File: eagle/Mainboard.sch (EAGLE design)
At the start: 34 parts, among them IC1 L293D, IC2 TLC272P, IC3 LM1085IT-5.0

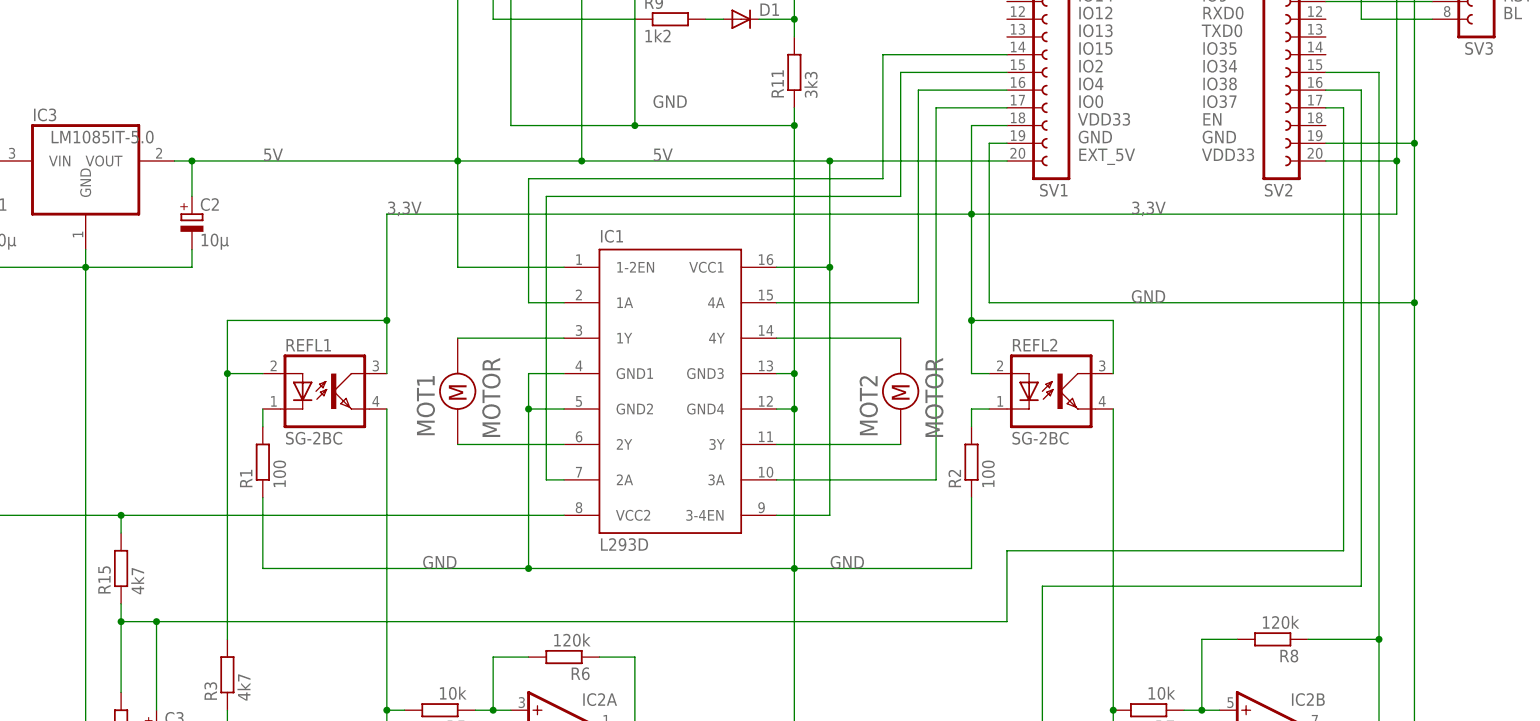
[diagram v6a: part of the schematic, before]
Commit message: 5V-Jumper hinzugefügt und Spanungsteiler für Akkumessung angepasst
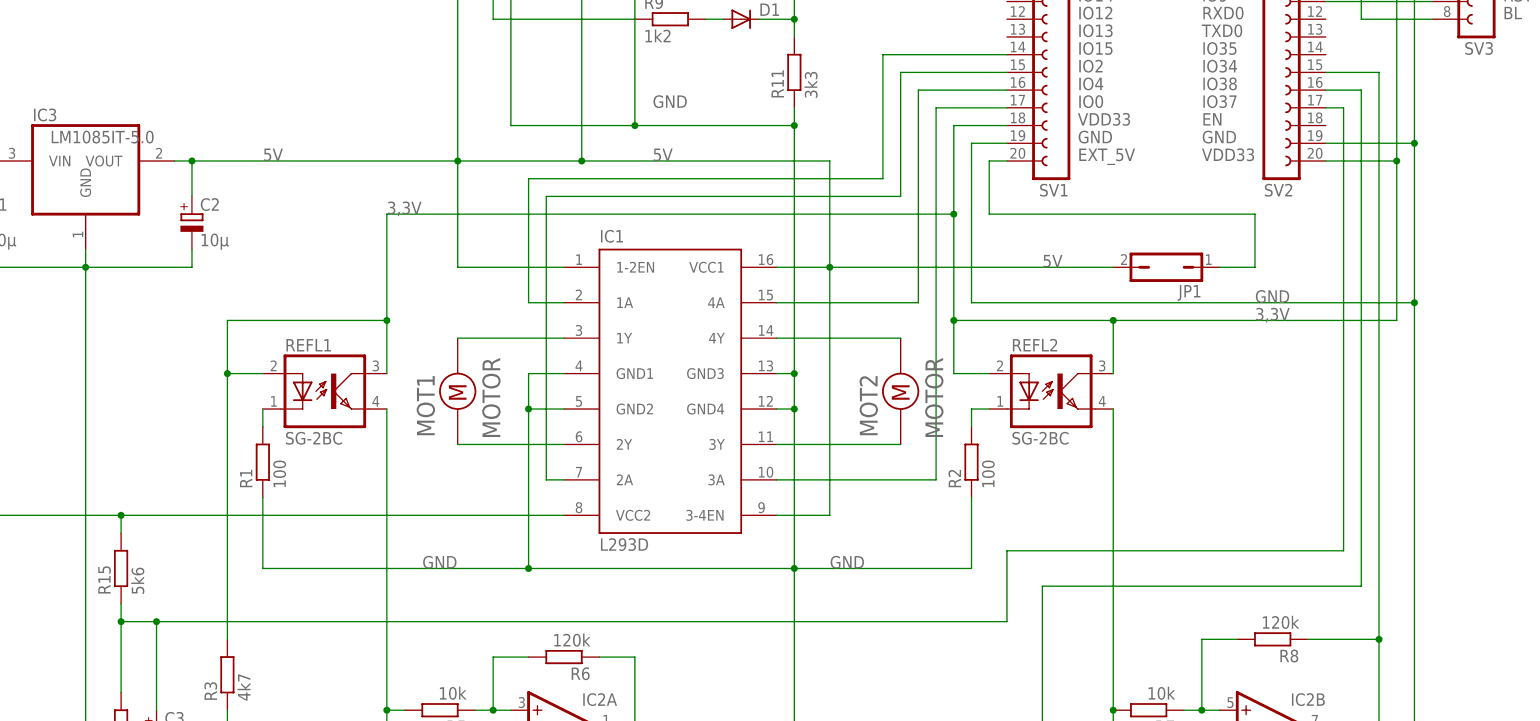
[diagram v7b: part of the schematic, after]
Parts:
- added JP1: (no value), jumper:JP1Q
- R15: value 4k7 -> 5k6
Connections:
- new net N$27: JP1.1, SV1.20
- net 5V: now also JP1.2; no longer SV1.20
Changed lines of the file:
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@@
 <part name="C3" library="rcl" library_urn="urn:adsk.eagle:library:334" deviceset="CPOL-EU" device="E3.5-10" package3d_urn="urn:adsk.eagle:package:23351/1" value="10µ"/>
 <part name="R14" library="rcl" library_urn="urn:adsk.eagle:library:334" deviceset="R-EU_" device="RDH/15" package3d_urn="urn:adsk.eagle:package:23595/1" value="3k3"/>
-<part name="R15" library="rcl" library_urn="urn:adsk.eagle:library:334" deviceset="R-EU_" device="RDH/15" package3d_urn="urn:adsk.eagle:package:23595/1" value="4k7"/>
+<part name="R15" library="rcl" library_urn="urn:adsk.eagle:library:334" deviceset="R-EU_" device="RDH/15" package3d_urn="urn:adsk.eagle:package:23595/1" value="5k6"/>
+<part name="JP1" library="jumper" library_urn="urn:adsk.eagle:library:252" deviceset="JP1Q" device="" package3d_urn="urn:adsk.eagle:package:15455/1"/>
 </parts>
 <sheets>
@@
 <instance part="R14" gate="G$1" x="25.4" y="25.4" rot="R90"/>
 <instance part="R15" gate="G$1" x="25.4" y="48.26" rot="R90"/>
+<instance part="JP1" gate="A" x="175.26" y="91.44" rot="R90"/>
 </instances>
 <busses>
@@
 <wire x1="121.92" y1="48.26" x2="147.32" y2="48.26" width="0.1524" layer="91"/>
 <wire x1="147.32" y1="48.26" x2="147.32" y2="58.42" width="0.1524" layer="91"/>
-<wire x1="149.86" y1="86.36" x2="210.82" y2="86.36" width="0.1524" layer="91"/>
+<wire x1="147.32" y1="86.36" x2="210.82" y2="86.36" width="0.1524" layer="91"/>
 <wire x1="210.82" y1="86.36" x2="210.82" y2="109.22" width="0.1524" layer="91"/>
 <pinref part="SV2" gate="G$1" pin="19"/>
@@
 <wire x1="210.82" y1="142.24" x2="213.36" y2="142.24" width="0.1524" layer="91"/>
 <pinref part="SV1" gate="G$1" pin="19"/>
-<wire x1="152.4" y1="109.22" x2="149.86" y2="109.22" width="0.1524" layer="91"/>
-<wire x1="149.86" y1="86.36" x2="149.86" y2="109.22" width="0.1524" layer="91"/>
-<label x="170.18" y="86.36" size="1.778" layer="95"/>
+<wire x1="152.4" y1="109.22" x2="147.32" y2="109.22" width="0.1524" layer="91"/>
+<wire x1="147.32" y1="86.36" x2="147.32" y2="109.22" width="0.1524" layer="91"/>
+<label x="187.96" y="86.36" size="1.778" layer="95"/>
 <label x="149.86" y="5.08" size="1.778" layer="95"/>
 <pinref part="R11" gate="G$1" pin="1"/>
@@
 <wire x1="35.56" y1="106.68" x2="73.66" y2="106.68" width="0.1524" layer="91"/>
 <wire x1="73.66" y1="106.68" x2="91.44" y2="106.68" width="0.1524" layer="91"/>
-<pinref part="SV1" gate="G$1" pin="20"/>
 <wire x1="91.44" y1="106.68" x2="127" y2="106.68" width="0.1524" layer="91"/>
-<wire x1="127" y1="106.68" x2="152.4" y2="106.68" width="0.1524" layer="91"/>
-<junction x="127" y="106.68"/>
 <pinref part="US1" gate="A" pin="1"/>
 <wire x1="73.66" y1="149.86" x2="73.66" y2="106.68" width="0.1524" layer="91"/>
@@
 <wire x1="35.56" y1="101.6" x2="35.56" y2="106.68" width="0.1524" layer="91"/>
 <junction x="35.56" y="106.68"/>
+<pinref part="JP1" gate="A" pin="2"/>
+<wire x1="127" y1="91.44" x2="167.64" y2="91.44" width="0.1524" layer="91"/>
+<label x="157.48" y="91.44" size="1.778" layer="95"/>
 </segment>
 </net>
@@
 <segment>
 <pinref part="SV1" gate="G$1" pin="18"/>
-<wire x1="152.4" y1="111.76" x2="147.32" y2="111.76" width="0.1524" layer="91"/>
-<wire x1="147.32" y1="111.76" x2="147.32" y2="99.06" width="0.1524" layer="91"/>
-<wire x1="147.32" y1="99.06" x2="208.28" y2="99.06" width="0.1524" layer="91"/>
-<wire x1="208.28" y1="99.06" x2="208.28" y2="106.68" width="0.1524" layer="91"/>
+<wire x1="152.4" y1="111.76" x2="144.78" y2="111.76" width="0.1524" layer="91"/>
+<wire x1="144.78" y1="111.76" x2="144.78" y2="99.06" width="0.1524" layer="91"/>
 <pinref part="SV2" gate="G$1" pin="20"/>
 <wire x1="208.28" y1="106.68" x2="198.12" y2="106.68" width="0.1524" layer="91"/>
@@
 <wire x1="63.5" y1="99.06" x2="63.5" y2="83.82" width="0.1524" layer="91"/>
 <wire x1="63.5" y1="83.82" x2="63.5" y2="76.2" width="0.1524" layer="91"/>
-<wire x1="147.32" y1="99.06" x2="63.5" y2="99.06" width="0.1524" layer="91"/>
-<junction x="147.32" y="99.06"/>
+<wire x1="144.78" y1="99.06" x2="63.5" y2="99.06" width="0.1524" layer="91"/>
+<junction x="144.78" y="99.06"/>
 <pinref part="REFL2" gate="G$1" pin="A"/>
-<wire x1="149.86" y1="76.2" x2="147.32" y2="76.2" width="0.1524" layer="91"/>
-<wire x1="147.32" y1="76.2" x2="147.32" y2="83.82" width="0.1524" layer="91"/>
-<wire x1="147.32" y1="83.82" x2="167.64" y2="83.82" width="0.1524" layer="91"/>
+<wire x1="149.86" y1="76.2" x2="144.78" y2="76.2" width="0.1524" layer="91"/>
+<wire x1="144.78" y1="76.2" x2="144.78" y2="83.82" width="0.1524" layer="91"/>
+<wire x1="144.78" y1="83.82" x2="167.64" y2="83.82" width="0.1524" layer="91"/>
 <wire x1="167.64" y1="83.82" x2="167.64" y2="76.2" width="0.1524" layer="91"/>
 <pinref part="REFL2" gate="G$1" pin="COL"/>
-<wire x1="147.32" y1="99.06" x2="147.32" y2="83.82" width="0.1524" layer="91"/>
-<junction x="147.32" y="83.82"/>
-<label x="170.18" y="99.06" size="1.778" layer="95"/>
+<wire x1="144.78" y1="99.06" x2="144.78" y2="83.82" width="0.1524" layer="91"/>
+<junction x="144.78" y="83.82"/>
+<label x="187.96" y="83.82" size="1.778" layer="95"/>
 <wire x1="208.28" y1="106.68" x2="208.28" y2="144.78" width="0.1524" layer="91"/>
 <junction x="208.28" y="106.68"/>
@@
 <wire x1="40.64" y1="83.82" x2="63.5" y2="83.82" width="0.1524" layer="91"/>
 <junction x="63.5" y="83.82"/>
+<wire x1="167.64" y1="83.82" x2="208.28" y2="83.82" width="0.1524" layer="91"/>
+<junction x="167.64" y="83.82"/>
+<wire x1="208.28" y1="83.82" x2="208.28" y2="106.68" width="0.1524" layer="91"/>
 </segment>
 </net>
@@
 </segment>
 </net>
+<net name="N$27" class="0">
+<segment>
+<pinref part="SV1" gate="G$1" pin="20"/>
+<wire x1="152.4" y1="106.68" x2="149.86" y2="106.68" width="0.1524" layer="91"/>
+<wire x1="149.86" y1="106.68" x2="149.86" y2="99.06" width="0.1524" layer="91"/>
+<wire x1="149.86" y1="99.06" x2="187.96" y2="99.06" width="0.1524" layer="91"/>
+<wire x1="187.96" y1="99.06" x2="187.96" y2="91.44" width="0.1524" layer="91"/>
+<pinref part="JP1" gate="A" pin="1"/>
+<wire x1="187.96" y1="91.44" x2="182.88" y2="91.44" width="0.1524" layer="91"/>
+</segment>
+</net>

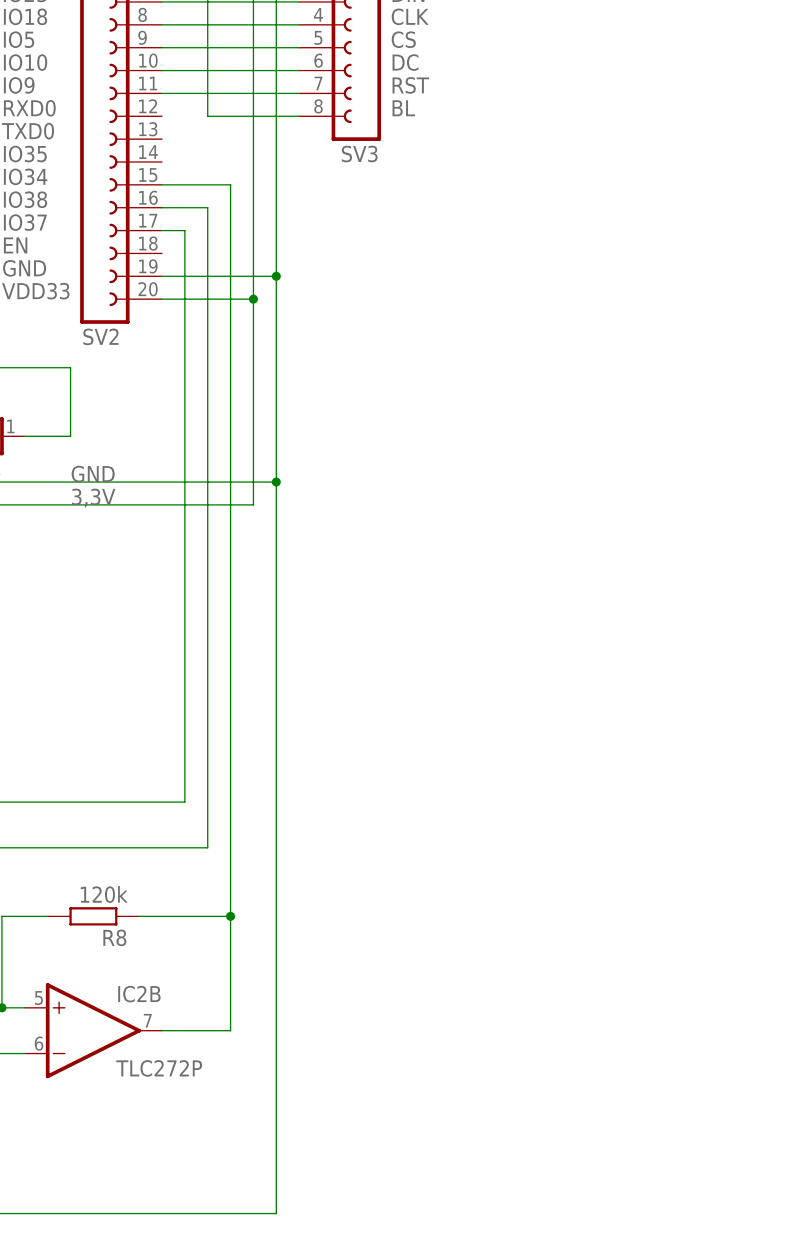
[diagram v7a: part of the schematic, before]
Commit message: Wassersensor hinzugefügt
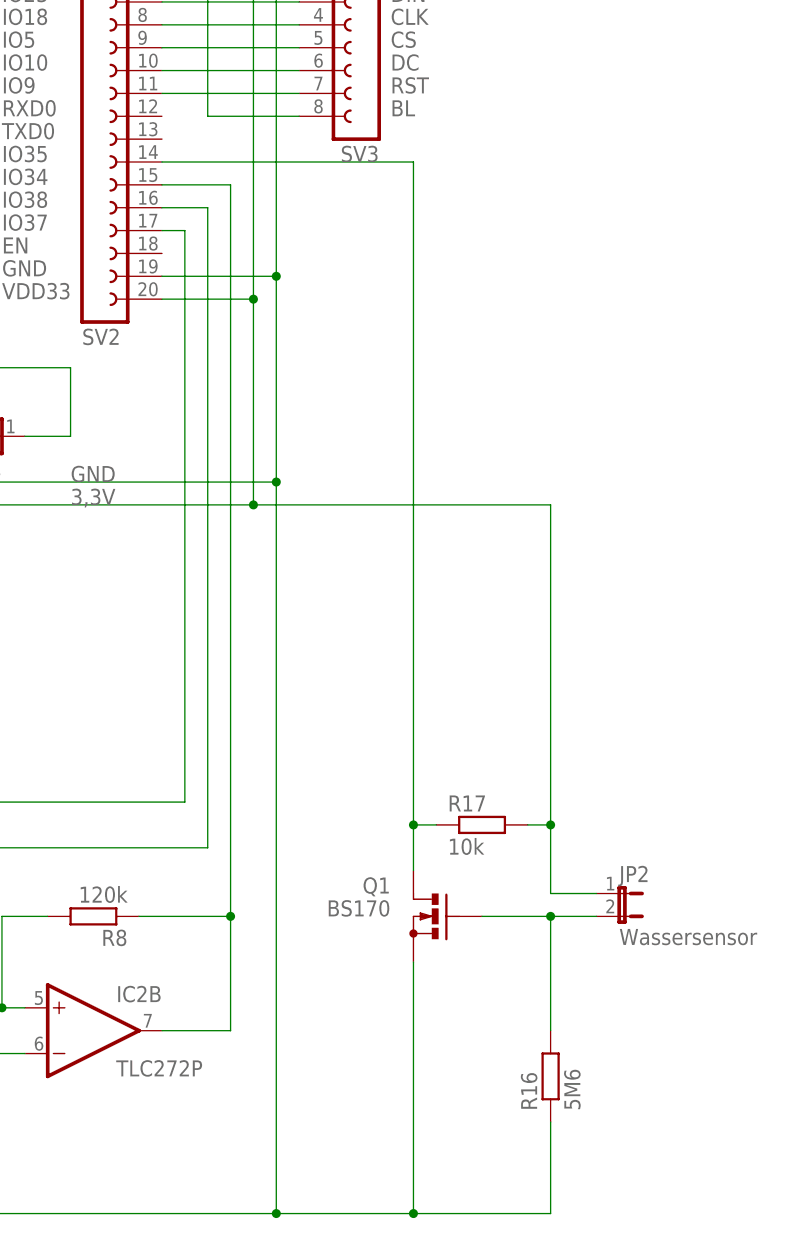
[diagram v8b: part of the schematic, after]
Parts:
- added JP2: Wassersensor, jumper:JP1E
- added Q1: BS170, transistor-small-signal:BS170
- added R16: 5M6, rcl:R-EU_RDH/15
- added R17: 10k, rcl:R-EU_RDH/15
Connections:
- new net N$34: Q1.D, R17.1, SV2.14
- new net N$35: JP2.2, Q1.G, R16.2
- net 3,3V: now also JP2.1, R17.2
- net GND: now also Q1.S, R16.1
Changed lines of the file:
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@@
 <part name="R15" library="rcl" library_urn="urn:adsk.eagle:library:334" deviceset="R-EU_" device="RDH/15" package3d_urn="urn:adsk.eagle:package:23595/1" value="5k6"/>
 <part name="JP1" library="jumper" library_urn="urn:adsk.eagle:library:252" deviceset="JP1Q" device="" package3d_urn="urn:adsk.eagle:package:15455/1"/>
+<part name="Q1" library="transistor-small-signal" library_urn="urn:adsk.eagle:library:401" deviceset="BS170" device="" package3d_urn="urn:adsk.eagle:package:29751/1"/>
+<part name="R16" library="rcl" library_urn="urn:adsk.eagle:library:334" deviceset="R-EU_" device="RDH/15" package3d_urn="urn:adsk.eagle:package:23595/1" value="5M6"/>
+<part name="JP2" library="jumper" library_urn="urn:adsk.eagle:library:252" deviceset="JP1E" device="" package3d_urn="urn:adsk.eagle:package:15455/1" value="Wassersensor"/>
+<part name="R17" library="rcl" library_urn="urn:adsk.eagle:library:334" deviceset="R-EU_" device="RDH/15" package3d_urn="urn:adsk.eagle:package:23595/1" value="10k"/>
 </parts>
 <sheets>
@@
 <instance part="R15" gate="G$1" x="25.4" y="48.26" rot="R90"/>
 <instance part="JP1" gate="A" x="175.26" y="91.44" rot="R90"/>
+<instance part="Q1" gate="1" x="228.6" y="38.1" rot="MR0"/>
+<instance part="R16" gate="G$1" x="241.3" y="20.32" rot="R90"/>
+<instance part="JP2" gate="A" x="248.92" y="40.64" rot="R270"/>
+<instance part="R17" gate="G$1" x="233.68" y="48.26"/>
 </instances>
 <busses>
@@
 <wire x1="25.4" y1="20.32" x2="25.4" y2="5.08" width="0.1524" layer="91"/>
 <junction x="25.4" y="5.08"/>
+<pinref part="Q1" gate="1" pin="S"/>
+<wire x1="226.06" y1="33.02" x2="226.06" y2="5.08" width="0.1524" layer="91"/>
+<wire x1="226.06" y1="5.08" x2="210.82" y2="5.08" width="0.1524" layer="91"/>
+<junction x="210.82" y="5.08"/>
+<pinref part="R16" gate="G$1" pin="1"/>
+<wire x1="226.06" y1="5.08" x2="241.3" y2="5.08" width="0.1524" layer="91"/>
+<wire x1="241.3" y1="5.08" x2="241.3" y2="15.24" width="0.1524" layer="91"/>
+<junction x="226.06" y="5.08"/>
 </segment>
 </net>
@@
 <junction x="167.64" y="83.82"/>
 <wire x1="208.28" y1="83.82" x2="208.28" y2="106.68" width="0.1524" layer="91"/>
+<wire x1="208.28" y1="83.82" x2="241.3" y2="83.82" width="0.1524" layer="91"/>
+<wire x1="241.3" y1="83.82" x2="241.3" y2="48.26" width="0.1524" layer="91"/>
+<junction x="208.28" y="83.82"/>
+<pinref part="JP2" gate="A" pin="1"/>
+<wire x1="241.3" y1="48.26" x2="241.3" y2="40.64" width="0.1524" layer="91"/>
+<wire x1="241.3" y1="40.64" x2="246.38" y2="40.64" width="0.1524" layer="91"/>
+<pinref part="R17" gate="G$1" pin="2"/>
+<wire x1="238.76" y1="48.26" x2="241.3" y2="48.26" width="0.1524" layer="91"/>
+<junction x="241.3" y="48.26"/>
 </segment>
 </net>
@@
 </segment>
 </net>
+<net name="N$34" class="0">
+<segment>
+<pinref part="SV2" gate="G$1" pin="14"/>
+<pinref part="Q1" gate="1" pin="D"/>
+<wire x1="198.12" y1="121.92" x2="226.06" y2="121.92" width="0.1524" layer="91"/>
+<wire x1="226.06" y1="121.92" x2="226.06" y2="48.26" width="0.1524" layer="91"/>
+<pinref part="R17" gate="G$1" pin="1"/>
+<wire x1="226.06" y1="48.26" x2="226.06" y2="43.18" width="0.1524" layer="91"/>
+<wire x1="228.6" y1="48.26" x2="226.06" y2="48.26" width="0.1524" layer="91"/>
+<junction x="226.06" y="48.26"/>
+</segment>
+</net>
+<net name="N$35" class="0">
+<segment>
+<pinref part="Q1" gate="1" pin="G"/>
+<pinref part="JP2" gate="A" pin="2"/>
+<wire x1="233.68" y1="38.1" x2="241.3" y2="38.1" width="0.1524" layer="91"/>
+<pinref part="R16" gate="G$1" pin="2"/>
+<wire x1="241.3" y1="38.1" x2="246.38" y2="38.1" width="0.1524" layer="91"/>
+<wire x1="241.3" y1="25.4" x2="241.3" y2="38.1" width="0.1524" layer="91"/>
+<junction x="241.3" y="38.1"/>
+</segment>
+</net>
